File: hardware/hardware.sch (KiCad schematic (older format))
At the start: 24 parts, among them J1 Screw_Terminal_1x12, P1 CONN_02X20, Q1 PN2222A, U1 74LS08, U2 AP111715, U3 74HC595, U4 LM555N, U5 DAC08, U6 LM555N

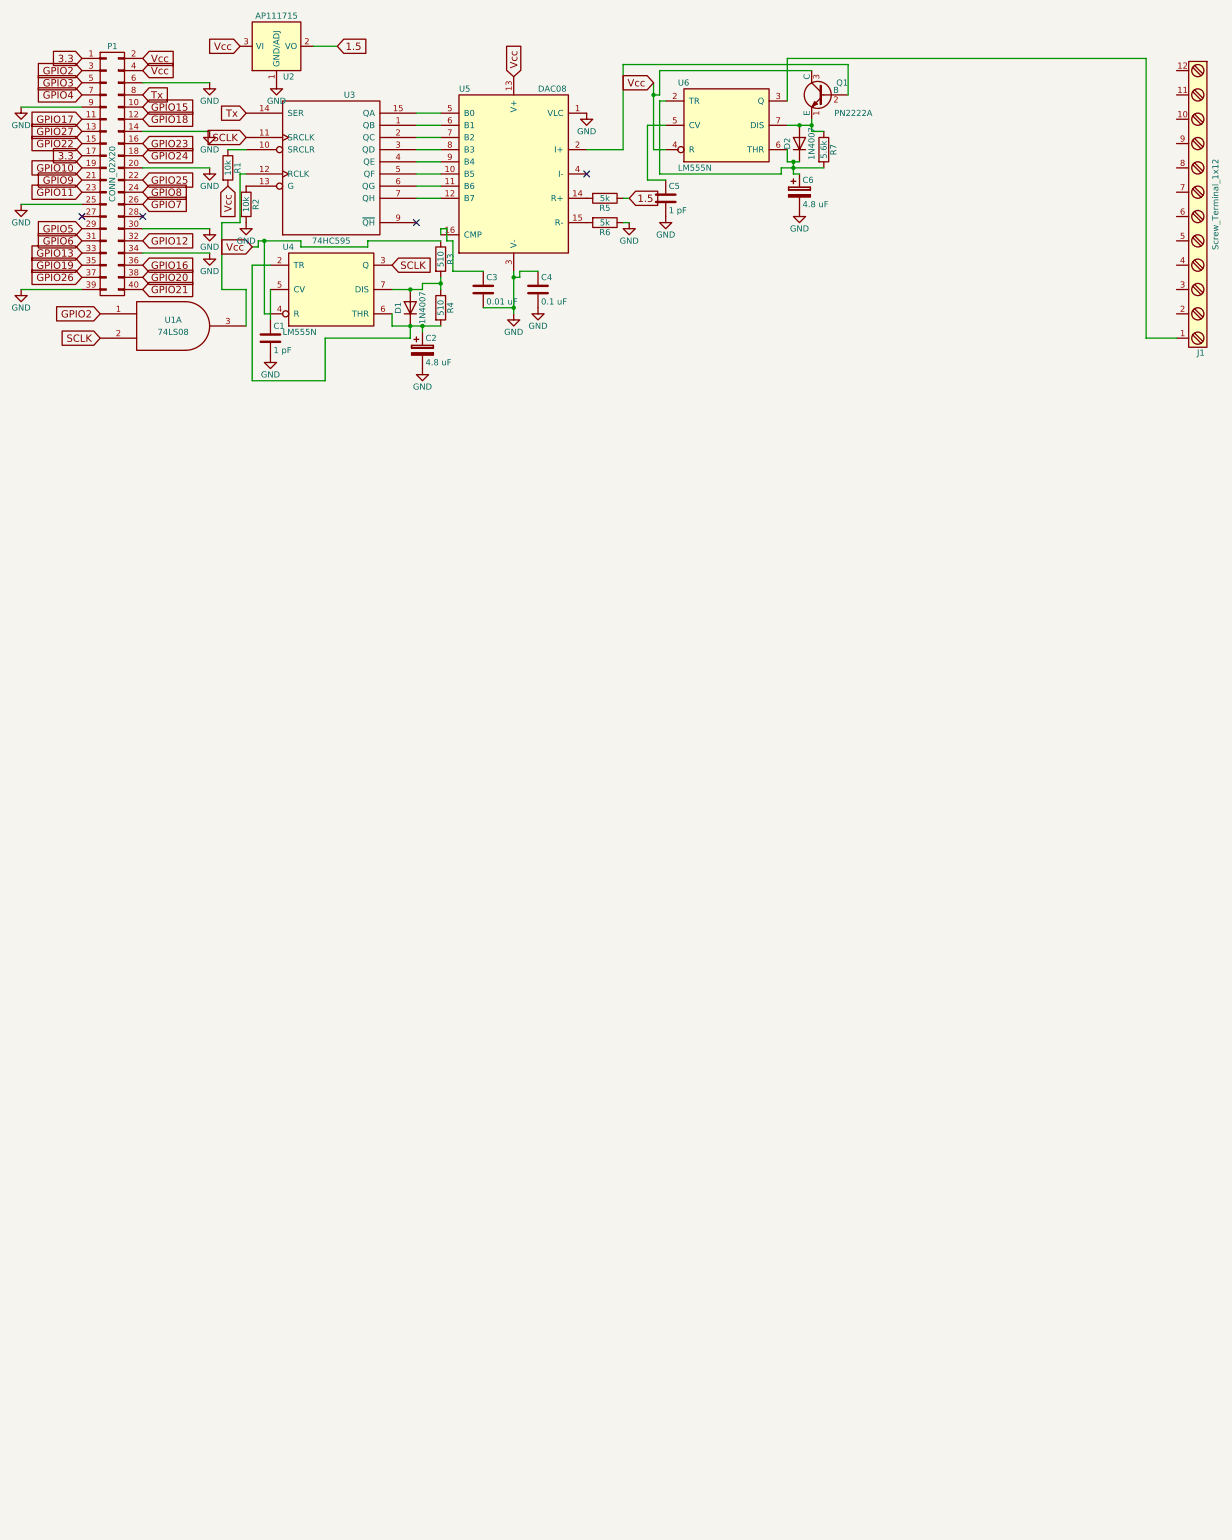
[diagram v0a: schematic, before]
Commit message: Finished first 7 PWM controllers
Note that these are entirely analog, and will probably require tuning on
the prototype.

Signed-off-by: Nkeck720 <noahkeck72@gmail.com>
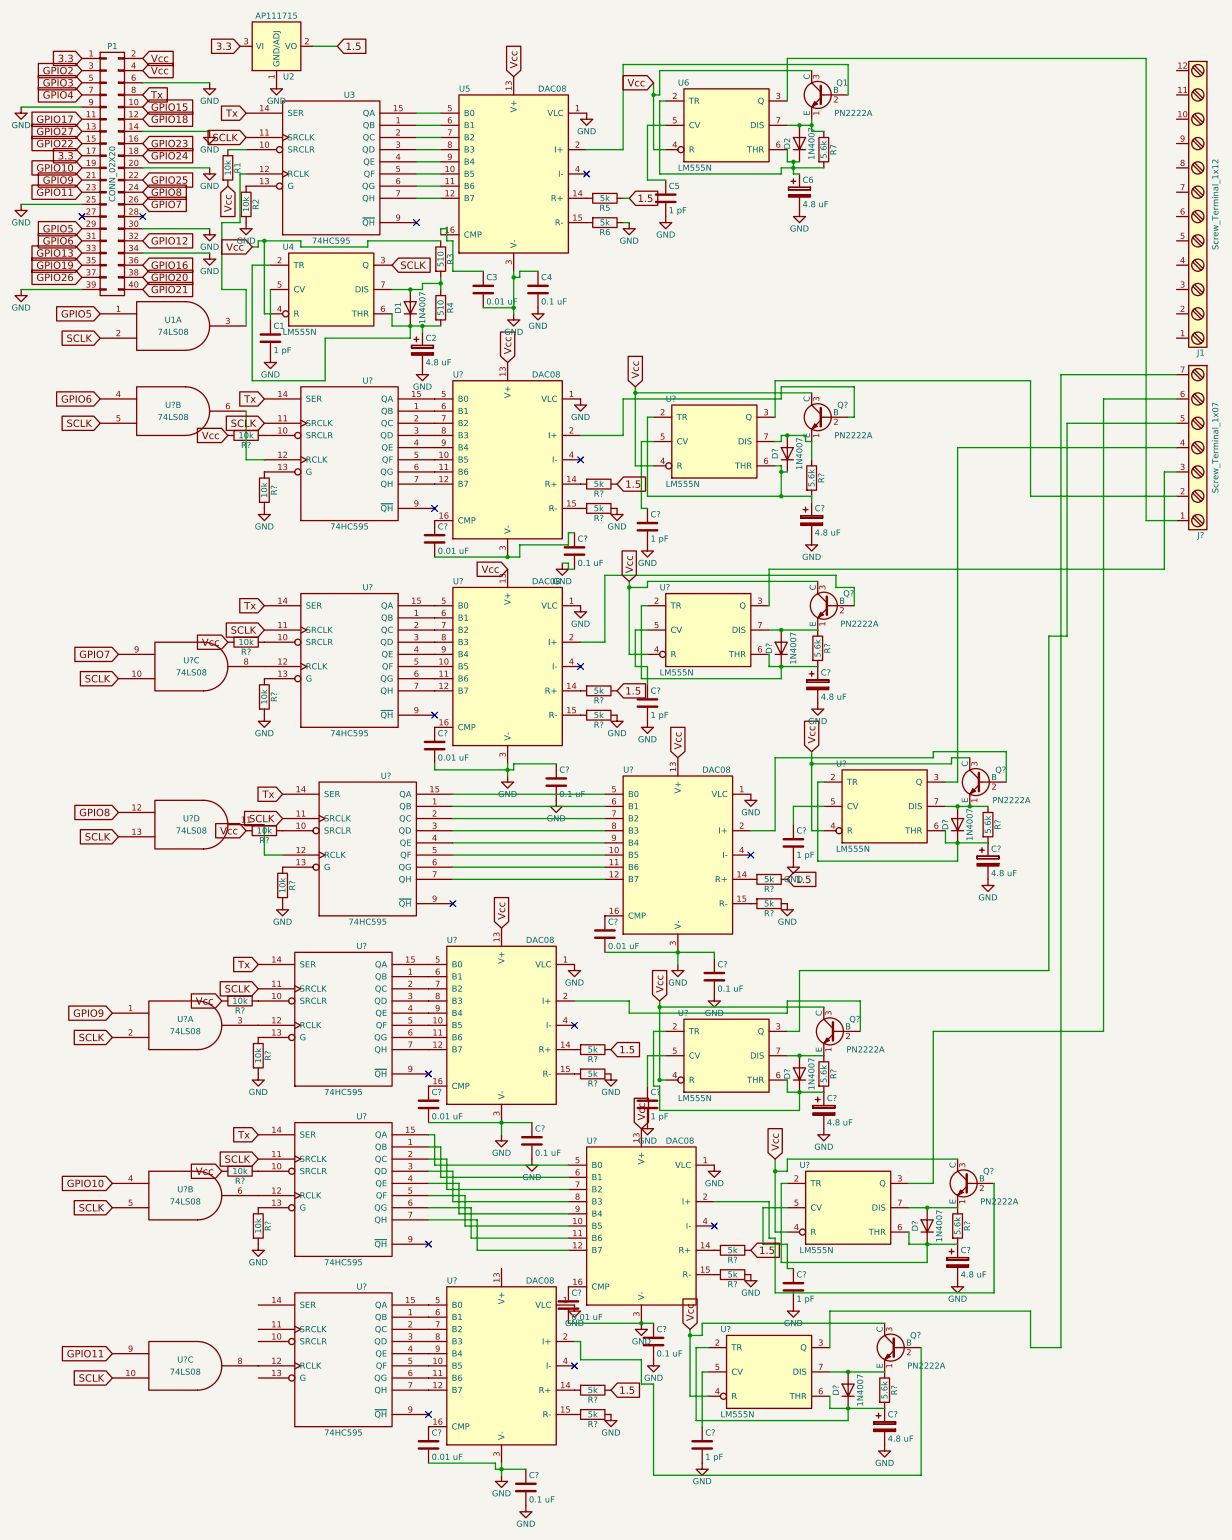
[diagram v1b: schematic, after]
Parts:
- added C? (x6): 0.1 uF, symbol C
- added C? (x6): 0.01 uF, symbol C
- added C? (x6): 4.8 uF, symbol CP
- added C? (x6): 1 pF, symbol C
- added D? (x6): 1N4007, symbol D
- added J?: Screw_Terminal_1x07, symbol Screw_Terminal_1x07
- added Q? (x6): PN2222A, symbol PN2222A
- added R? (x10): 10k, symbol R
- added R? (x12): 5k, symbol R
- added R? (x6): 5.6k, symbol R
- added U? (x6): 74LS08, symbol 74LS08
- added U? (x6): 74HC595, symbol 74HC595
- added U? (x6): DAC08, symbol DAC08
- added U? (x6): LM555N, symbol LM555N
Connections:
- net 1.5: now also R?.1, R?.1, R?.1, R?.1, R?.1, R?.1
- net 3.3: now also U2.3 (VI)
- net GND: now also C?.1, C?.1, C?.1, C?.1, C?.1, C?.2, C?.2, C?.2, C?.2, C?.2, C?.2, C?.2, C?.2, C?.2, C?.2, C?.2, C?.2, C?.2, C?.2, C?.2, C?.2, C?.2, C?.2, C?.2, C?.2, C?.2, C?.2, C?.2, R?.1, R?.1, R?.1, R?.1, R?.1, R?.1, R?.2, R?.2, R?.2, R?.2, R?.2, U?.1 (GND), U?.1 (GND), U?.1 (GND), U?.1 (GND), U?.1 (GND), U?.1 (GND), U?.1 (VLC), U?.1 (VLC), U?.1 (VLC), U?.1 (VLC), U?.1 (VLC), U?.1 (VLC), U?.3 (V-), U?.3 (V-), U?.3 (V-), U?.3 (V-), U?.3 (V-), U?.7 (GND), U?.7 (GND), U?.7 (GND), U?.7 (GND), U?.7 (GND), U?.7 (GND), U?.8 (GND), U?.8 (GND), U?.8 (GND), U?.8 (GND), U?.8 (GND), U?.8 (GND)
- net GPIO10: now also U?.4
- net GPIO11: now also U?.9
- net GPIO2: no longer U1.1
- net GPIO5: now also U1.1
- net GPIO6: now also U?.4
- net GPIO7: now also U?.9
- net GPIO8: now also U?.12
- net GPIO9: now also U?.1
- net SCLK: now also U?.10, U?.10, U?.11 (SRCLK), U?.11 (SRCLK), U?.11 (SRCLK), U?.11 (SRCLK), U?.11 (SRCLK), U?.13, U?.2, U?.5, U?.5
- net Tx: now also U?.14 (SER), U?.14 (SER), U?.14 (SER), U?.14 (SER), U?.14 (SER)
- net VCC: now also U?.14 (VCC), U?.14 (VCC), U?.14 (VCC), U?.14 (VCC), U?.14 (VCC), U?.14 (VCC), U?.16 (VCC), U?.16 (VCC), U?.16 (VCC), U?.16 (VCC), U?.16 (VCC), U?.16 (VCC), U?.8 (VCC), U?.8 (VCC), U?.8 (VCC), U?.8 (VCC), U?.8 (VCC), U?.8 (VCC)
- net Vcc: now also Q?.3 (C), Q?.3 (C), Q?.3 (C), Q?.3 (C), Q?.3 (C), Q?.3 (C), R?.2, R?.2, R?.2, R?.2, R?.2, U?.13 (V+), U?.13 (V+), U?.13 (V+), U?.13 (V+), U?.13 (V+), U?.4 (R), U?.4 (R), U?.4 (R), U?.4 (R), U?.4 (R), U?.4 (R); no longer U2.3 (VI)
- net at U6.3 (Q): now also J?.1; no longer J1.1
- new net: U?.12 (RCLK), U?.6 (x2)
- new net: U?.1 (QB), U?.6 (B1) (x6)
- new net: R?.1, U?.10 (SRCLR) (x5)
- new net: R?.1, U?.13 (G) (x5)
- new net: U?.15 (QA), U?.5 (B0) (x6)
- new net: U?.2 (QC), U?.7 (B2) (x6)
- new net: U?.3 (QD), U?.8 (B3) (x6)
- new net: U?.4 (QE), U?.9 (B4) (x6)
- new net: U?.10 (B5), U?.5 (QF) (x6)
- new net: U?.11 (B6), U?.6 (QG) (x6)
- new net: U?.12 (B7), U?.7 (QH) (x6)
- new net: R?.2, U?.14 (R+) (x6)
- new net: R?.2, U?.15 (R-) (x6)
- new net: C?.1, U?.16 (CMP) (x6)
- new net: Q?.2 (B), U?.2 (I+) (x6)
- new net: C?.1, C?.2, U?.3 (V-)
- new net: C?.1, D?.1 (K), R?.2, U?.2 (TR), U?.6 (THR) (x6)
- new net: J?.2, U?.3 (Q)
- new net: C?.1, U?.5 (CV) (x6)
- new net: D?.2 (A), Q?.1 (E), R?.1, U?.7 (DIS) (x6)
- new net: J?.3, U?.3 (Q)
- new net: J?.4, U?.3 (Q)
- new net: J?.5, U?.3 (Q)
- new net: J?.6, U?.3 (Q)
- new net: J?.7, U?.3 (Q)
- new net: U?.12 (RCLK), U?.8 (x2)
- new net: U?.11, U?.12 (RCLK)
- new net: U?.12 (RCLK), U?.3
- no-connect marks 4 -> 16

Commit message: Tied up loose ends
Only have three more PWM controllers to go.
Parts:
- added C10, C17, C18, C20, C51, C52, C55, C56, C7: 0.01 uF, Capacitors_SMD:C_0603_HandSoldering, symbol C
- added C13, C15, C24, C28, C29, C53, C54, C57, C58: 0.1 uF, Capacitors_SMD:C_0603_HandSoldering, symbol C
- added C31, C32, C35, C38, C39, C59, C60, C61, C62: 1 pF, Capacitors_SMD:C_0603_HandSoldering, symbol C
- added C43, C44, C46, C48, C49, C63, C64, C65, C66: 4.8 uF, Capacitors_SMD:CP_Elec_5x5.8, symbol CP
- added D11, D12, D14, D15, D16, D17, D6, D7, D9: 1N4007, Diodes_THT:D_DO-41_SOD81_P7.62mm_Horizontal, symbol D
- added Q10, Q12, Q13, Q14, Q15, Q16, Q5, Q6, Q8: PN2222A, TO_SOT_Packages_THT:TO-92_Rugged, symbol PN2222A
- added R10, R13, R14, R15, R18, R19, R20, R23, R24, R25, R63, R64, R65, R66, R67, R68, R69, R70, R8, R9: 10k, Resistors_SMD:R_0805_HandSoldering, symbol R
- added R30, R31, R36, R37, R42, R43, R44, R45, R46, R47, R71, R72, R73, R74, R75, R76, R77, R78: 5k, Resistors_SMD:R_0805_HandSoldering, symbol R
- added R55, R56, R58, R60, R61, R79, R80, R81, R82: 5.6k, Resistors_SMD:R_0805_HandSoldering, symbol R
- added unit 3 of U1
- added unit 4 of U1
- added U10, U11, U15, U16, U43, U44, U45, U46, U9: 74HC595, Housings_DIP:DIP-16_W7.62mm, symbol 74HC595
- added U20, U23, U26, U27, U28, U47, U48, U49, U50: DAC08, Housings_DIP:DIP-16_W7.62mm, symbol DAC08
- added U34, U35, U37, U39, U40, U51, U52, U53, U54: LM555N, Housings_DIP:DIP-8_W7.62mm, symbol LM555N
- added U42: 74LS08, Housings_DIP:DIP-14_W7.62mm, symbol 74LS08
- added unit 1 of U7
- added unit 1 of U8
- added unit 2 of U8
- C1, C3, C4, C5: footprint (none) -> Capacitors_SMD:C_0603_HandSoldering
- C11, C12, C14, C16, C19, C21, C22, C23, C25, C26, C27, C30, C33, C34, C36, C37, C8, C9: renamed from C?; footprint (none) -> Capacitors_SMD:C_0603_HandSoldering
- C2, C6: footprint (none) -> Capacitors_SMD:CP_Elec_5x5.8
- C40, C41, C42, C45, C47, C50: renamed from C?; footprint (none) -> Capacitors_SMD:CP_Elec_5x5.8
- D1, D2: footprint (none) -> Diodes_THT:D_DO-41_SOD81_P7.62mm_Horizontal
- D10, D13, D3, D4, D5, D8: renamed from D?; footprint (none) -> Diodes_THT:D_DO-41_SOD81_P7.62mm_Horizontal
- J1: footprint (none) -> Connectors_Terminal_Blocks:TerminalBlock_Pheonix_MKDS1.5-12pol
- J2: renamed from J?; footprint (none) -> Connectors_Terminal_Blocks:TerminalBlock_Pheonix_MKDS1.5-7pol
- P1: footprint (none) -> Pin_Headers:Pin_Header_Straight_2x20_Pitch2.54mm
- Q1: footprint (none) -> TO_SOT_Packages_THT:TO-92_Rugged
- Q11, Q2, Q3, Q4, Q7, Q9: renamed from Q?; footprint (none) -> TO_SOT_Packages_THT:TO-92_Rugged
- R1, R2, R5, R6, R7: footprint (none) -> Resistors_SMD:R_0805_HandSoldering
- R11, R12, R16, R17, R21, R22, R26, R27, R28, R29, R32, R33, R34, R35, R38, R39, R40, R41, R48, R49, R50, R51, R52, R53, R54, R57, R59, R62: renamed from R?; footprint (none) -> Resistors_SMD:R_0805_HandSoldering
- R3, R4: footprint (none) -> Resistors_THT:R_Axial_DIN0207_L6.3mm_D2.5mm_P7.62mm_Horizontal
- U1: footprint (none) -> Housings_DIP:DIP-14_W7.62mm
- U1, U7, U8: renamed from U?; footprint (none) -> Housings_DIP:DIP-14_W7.62mm
- U12, U13, U14, U17, U18, U19, U21, U22, U24, U25, U29, U30: renamed from U?; footprint (none) -> Housings_DIP:DIP-16_W7.62mm
- U3, U5: footprint (none) -> Housings_DIP:DIP-16_W7.62mm
- U31, U32, U33, U36, U38, U41: renamed from U?; footprint (none) -> Housings_DIP:DIP-8_W7.62mm
- U4, U6: footprint (none) -> Housings_DIP:DIP-8_W7.62mm
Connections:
- net 1.5: now also R30.1, R36.1, R42.1, R44.1, R46.1, R71.1, R73.1, R75.1, R77.1
- net GND: now also C10.2, C13.1, C13.2, C15.1, C15.2, C17.2, C18.2, C20.2, C24.1, C24.2, C28.1, C28.2, C29.1, C29.2, C31.2, C32.2, C35.2, C38.2, C39.2, C43.2, C44.2, C46.2, C48.2, C49.2, C51.2, C52.2, C53.1, C53.2, C54.1, C54.2, C55.2, C56.2, C57.1, C57.2, C58.1, C58.2, C59.2, C60.2, C61.2, C62.2, C63.2, C64.2, C65.2, C66.2, C7.2, R18.2, R19.2, R20.2, R23.2, R24.2, R25.2, R31.1, R37.1, R43.1, R45.1, R47.1, R67.2, R68.2, R69.2, R70.2, R72.1, R74.1, R76.1, R78.1, U1.7 (GND), U1.7 (GND), U10.8 (GND), U11.8 (GND), U15.8 (GND), U16.8 (GND), U20.1 (VLC), U20.3 (V-), U23.1 (VLC), U23.3 (V-), U26.1 (VLC), U26.3 (V-), U27.1 (VLC), U27.3 (V-), U28.1 (VLC), U28.3 (V-), U34.1 (GND), U35.1 (GND), U37.1 (GND), U39.1 (GND), U40.1 (GND), U42.7 (GND), U42.7 (GND), U42.7 (GND), U42.7 (GND), U43.8 (GND), U44.8 (GND), U45.8 (GND), U46.8 (GND), U47.1 (VLC), U47.3 (V-), U48.1 (VLC), U48.3 (V-), U49.1 (VLC), U49.3 (V-), U50.1 (VLC), U50.3 (V-), U51.1 (GND), U52.1 (GND), U53.1 (GND), U54.1 (GND), U7.7 (GND), U8.7 (GND), U8.7 (GND), U9.8 (GND)
- net GPIO10: now also U7.9; no longer U7.4
- net GPIO11: now also U7.12; no longer U7.9
- net GPIO12: now also U8.1
- net GPIO13: now also U8.4
- net GPIO15: now also U1.9
- net GPIO16: now also U1.12
- net GPIO17: now also U7.1
- net GPIO18: now also U42.1
- net GPIO19: now also U42.4
- net GPIO20: now also U42.12, U42.9
- net GPIO9: now also U7.4; no longer U7.1
- net SCLK: now also U14.11 (SRCLK), U7.10, U7.13, U7.5, U1.10, U1.13, U10.11 (SRCLK), U11.11 (SRCLK), U15.11 (SRCLK), U16.11 (SRCLK), U42.10, U42.13, U42.2, U42.5, U43.11 (SRCLK), U44.11 (SRCLK), U45.11 (SRCLK), U46.11 (SRCLK), U7.2, U8.2, U8.5, U9.11 (SRCLK); no longer U7.10, U7.2, U7.5
- net Tx: now also U14.14 (SER), U10.14 (SER), U11.14 (SER), U15.14 (SER), U16.14 (SER), U43.14 (SER), U44.14 (SER), U45.14 (SER), U46.14 (SER), U9.14 (SER)
- net VCC: now also U1.14 (VCC), U1.14 (VCC), U10.16 (VCC), U11.16 (VCC), U15.16 (VCC), U16.16 (VCC), U34.8 (VCC), U35.8 (VCC), U37.8 (VCC), U39.8 (VCC), U40.8 (VCC), U42.14 (VCC), U42.14 (VCC), U42.14 (VCC), U42.14 (VCC), U43.16 (VCC), U44.16 (VCC), U45.16 (VCC), U46.16 (VCC), U51.8 (VCC), U52.8 (VCC), U53.8 (VCC), U54.8 (VCC), U7.14 (VCC), U8.14 (VCC), U8.14 (VCC), U9.16 (VCC)
- net Vcc: now also U22.13 (V+), Q10.3 (C), Q12.3 (C), Q13.3 (C), Q14.3 (C), Q15.3 (C), Q16.3 (C), Q5.3 (C), Q6.3 (C), Q8.3 (C), R10.2, R13.2, R14.2, R15.2, R63.2, R64.2, R65.2, R66.2, R8.2, R9.2, U20.13 (V+), U23.13 (V+), U26.13 (V+), U27.13 (V+), U28.13 (V+), U34.4 (R), U35.4 (R), U37.4 (R), U39.4 (R), U40.4 (R), U47.13 (V+), U48.13 (V+), U49.13 (V+), U50.13 (V+), U51.4 (R), U52.4 (R), U53.4 (R), U54.4 (R)
- net at J1.1: now also U40.3 (Q)
- net at J1.2: now also U34.3 (Q)
- net at J1.3: now also U39.3 (Q)
- net at J1.4: now also U35.3 (Q)
- net at J1.5: now also U37.3 (Q)
- net at J1.6: now also U51.3 (Q)
- net at J1.7: now also U54.3 (Q)
- net at J1.8: now also U52.3 (Q)
- net at J1.9: now also U53.3 (Q)
- net at U12.12 (RCLK): now also U7.6; no longer U7.3
- net at U13.12 (RCLK): now also U7.8; no longer U7.6
- net at U14.12 (RCLK): now also U7.11; no longer U7.8
- net at U14.10 (SRCLR): now also R13.1
- net at U14.13 (G): now also R23.1
- new net: U15.12 (RCLK), U8.3
- new net: U15.1 (QB), U28.6 (B1)
- new net: R14.1, U15.10 (SRCLR)
- new net: R24.1, U15.13 (G)
- new net: U15.15 (QA), U28.5 (B0)
- new net: U15.2 (QC), U28.7 (B2)
- new net: U15.3 (QD), U28.8 (B3)
- new net: U15.4 (QE), U28.9 (B4)
- new net: U15.5 (QF), U28.10 (B5)
- new net: U15.6 (QG), U28.11 (B6)
- new net: U15.7 (QH), U28.12 (B7)
- new net: R46.2, U28.14 (R+)
- new net: R47.2, U28.15 (R-)
- new net: C20.1, U28.16 (CMP)
- new net: Q12.2 (B), U28.2 (I+)
- new net: C49.1, D12.1 (K), R61.2, U40.2 (TR), U40.6 (THR)
- new net: C38.1, U40.5 (CV)
- new net: D12.2 (A), Q12.1 (E), R61.1, U40.7 (DIS)
- new net: U16.12 (RCLK), U8.6
- new net: U16.1 (QB), U23.6 (B1)
- new net: R15.1, U16.10 (SRCLR)
- new net: R25.1, U16.13 (G)
- new net: U16.15 (QA), U23.5 (B0)
- new net: U16.2 (QC), U23.7 (B2)
- new net: U16.3 (QD), U23.8 (B3)
- new net: U16.4 (QE), U23.9 (B4)
- new net: U16.5 (QF), U23.10 (B5)
- new net: U16.6 (QG), U23.11 (B6)
- new net: U16.7 (QH), U23.12 (B7)
- new net: R36.2, U23.14 (R+)
- new net: R37.2, U23.15 (R-)
- new net: C10.1, U23.16 (CMP)
- new net: Q5.2 (B), U23.2 (I+)
- new net: C43.1, D6.1 (K), R55.2, U34.2 (TR), U34.6 (THR)
- new net: C31.1, U34.5 (CV)
- new net: D6.2 (A), Q5.1 (E), R55.1, U34.7 (DIS)
- new net: U1.8, U9.12 (RCLK)
- new net: U27.6 (B1), U9.1 (QB)
- new net: R8.1, U9.10 (SRCLR)
- new net: R18.1, U9.13 (G)
- new net: U27.5 (B0), U9.15 (QA)
- new net: U27.7 (B2), U9.2 (QC)
- new net: U27.8 (B3), U9.3 (QD)
- new net: U27.9 (B4), U9.4 (QE)
- new net: U27.10 (B5), U9.5 (QF)
- new net: U27.11 (B6), U9.6 (QG)
- new net: U27.12 (B7), U9.7 (QH)
- new net: R44.2, U27.14 (R+)
- new net: R45.2, U27.15 (R-)
- new net: C18.1, U27.16 (CMP)
- new net: Q10.2 (B), U27.2 (I+)
- new net: C48.1, D11.1 (K), R60.2, U39.2 (TR), U39.6 (THR)
- new net: C39.1, U39.5 (CV)
- new net: D11.2 (A), Q10.1 (E), R60.1, U39.7 (DIS)
- new net: U1.11, U10.12 (RCLK)
- new net: U10.1 (QB), U20.6 (B1)
- new net: R9.1, U10.10 (SRCLR)
- new net: R19.1, U10.13 (G)
- new net: U10.15 (QA), U20.5 (B0)
- new net: U10.2 (QC), U20.7 (B2)
- new net: U10.3 (QD), U20.8 (B3)
- new net: U10.4 (QE), U20.9 (B4)
- new net: U10.5 (QF), U20.10 (B5)
- new net: U10.6 (QG), U20.11 (B6)
- new net: U10.7 (QH), U20.12 (B7)
- new net: R30.2, U20.14 (R+)
- new net: R31.2, U20.15 (R-)
- new net: C7.1, U20.16 (CMP)
- new net: Q6.2 (B), U20.2 (I+)
- new net: C44.1, D7.1 (K), R56.2, U35.2 (TR), U35.6 (THR)
- new net: C32.1, U35.5 (CV)
- new net: D7.2 (A), Q6.1 (E), R56.1, U35.7 (DIS)
- new net: U11.12 (RCLK), U7.3
- new net: U11.1 (QB), U26.6 (B1)
- new net: R10.1, U11.10 (SRCLR)
- new net: R20.1, U11.13 (G)
- new net: U11.15 (QA), U26.5 (B0)
- new net: U11.2 (QC), U26.7 (B2)
- new net: U11.3 (QD), U26.8 (B3)
- new net: U11.4 (QE), U26.9 (B4)
- new net: U11.5 (QF), U26.10 (B5)
- new net: U11.6 (QG), U26.11 (B6)
- new net: U11.7 (QH), U26.12 (B7)
- new net: R42.2, U26.14 (R+)
- new net: R43.2, U26.15 (R-)
- new net: C17.1, U26.16 (CMP)
- new net: Q8.2 (B), U26.2 (I+)
- new net: C46.1, D9.1 (K), R58.2, U37.2 (TR), U37.6 (THR)
- new net: C35.1, U37.5 (CV)
- new net: D9.2 (A), Q8.1 (E), R58.1, U37.7 (DIS)
- new net: U42.3, U43.12 (RCLK)
- new net: U43.1 (QB), U47.6 (B1)
- new net: R63.1, U43.10 (SRCLR)
- new net: R67.1, U43.13 (G)
- new net: U43.15 (QA), U47.5 (B0)
- new net: U43.2 (QC), U47.7 (B2)
- new net: U43.3 (QD), U47.8 (B3)
- new net: U43.4 (QE), U47.9 (B4)
- new net: U43.5 (QF), U47.10 (B5)
- new net: U43.6 (QG), U47.11 (B6)
- new net: U43.7 (QH), U47.12 (B7)
- new net: R71.2, U47.14 (R+)
- new net: R72.2, U47.15 (R-)
- new net: C51.1, U47.16 (CMP)
- new net: Q13.2 (B), U47.2 (I+)
- new net: C63.1, D14.1 (K), R79.2, U51.2 (TR), U51.6 (THR)
- new net: C60.1, U51.5 (CV)
- new net: D14.2 (A), Q13.1 (E), R79.1, U51.7 (DIS)
- new net: U42.6, U44.12 (RCLK)
- new net: U44.1 (QB), U50.6 (B1)
- new net: R64.1, U44.10 (SRCLR)
- new net: R68.1, U44.13 (G)
- new net: U44.15 (QA), U50.5 (B0)
- new net: U44.2 (QC), U50.7 (B2)
- new net: U44.3 (QD), U50.8 (B3)
- new net: U44.4 (QE), U50.9 (B4)
- new net: U44.5 (QF), U50.10 (B5)
- new net: U44.6 (QG), U50.11 (B6)
- new net: U44.7 (QH), U50.12 (B7)
- new net: R77.2, U50.14 (R+)
- new net: R78.2, U50.15 (R-)
- new net: C56.1, U50.16 (CMP)
- new net: Q16.2 (B), U50.2 (I+)
- new net: C66.1, D17.1 (K), R82.2, U54.2 (TR), U54.6 (THR)
- new net: C62.1, U54.5 (CV)
- new net: D17.2 (A), Q16.1 (E), R82.1, U54.7 (DIS)
- new net: U45.1 (QB), U48.6 (B1)
- new net: R65.1, U45.10 (SRCLR)
- new net: U42.8, U45.12 (RCLK)
- new net: R69.1, U45.13 (G)
- new net: U45.15 (QA), U48.5 (B0)
- new net: U45.2 (QC), U48.7 (B2)
- new net: U45.3 (QD), U48.8 (B3)
- new net: U45.4 (QE), U48.9 (B4)
- new net: U45.5 (QF), U48.10 (B5)
- new net: U45.6 (QG), U48.11 (B6)
- new net: U45.7 (QH), U48.12 (B7)
- new net: R73.2, U48.14 (R+)
- new net: R74.2, U48.15 (R-)
- new net: C52.1, U48.16 (CMP)
- new net: Q14.2 (B), U48.2 (I+)
- new net: C64.1, D15.1 (K), R80.2, U52.2 (TR), U52.6 (THR)
- new net: C59.1, U52.5 (CV)
- new net: D15.2 (A), Q14.1 (E), R80.1, U52.7 (DIS)
- new net: U42.11, U46.12 (RCLK)
- new net: U46.1 (QB), U49.6 (B1)
- new net: R66.1, U46.10 (SRCLR)
- new net: R70.1, U46.13 (G)
- new net: U46.15 (QA), U49.5 (B0)
- new net: U46.2 (QC), U49.7 (B2)
- new net: U46.3 (QD), U49.8 (B3)
- new net: U46.4 (QE), U49.9 (B4)
- new net: U46.5 (QF), U49.10 (B5)
- new net: U46.6 (QG), U49.11 (B6)
- new net: U46.7 (QH), U49.12 (B7)
- new net: R75.2, U49.14 (R+)
- new net: R76.2, U49.15 (R-)
- new net: C55.1, U49.16 (CMP)
- new net: Q15.2 (B), U49.2 (I+)
- new net: C65.1, D16.1 (K), R81.2, U53.2 (TR), U53.6 (THR)
- new net: C61.1, U53.5 (CV)
- new net: D16.2 (A), Q15.1 (E), R81.1, U53.7 (DIS)
- no-connect marks 16 -> 34
